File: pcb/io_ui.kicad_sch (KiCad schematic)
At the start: 66 parts, among them J10 UART, J4 Digital IO, J5 ADC Inputs, J8 I2C Bus, Q4 2N7002, Q5 2N7002, U8 24AA64T

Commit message: BOM: fill MPN/Manufacturer/LCSC for 47 Rev B parts (Basic preferred; C3 10u/25V, C7 1u/50V, C11 100n/50V). Hand-solder parts J11, Q3, Q8, DS1, L2 marked Assembly=hand solder and excluded from pos files. Nets unchanged, ERC 0 errors
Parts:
- C22: LCSC (none) -> C49678; MPN (none) -> CC0805KRX7R9BB104; Manufacturer (none) -> YAGEO
- DS1: Assembly (none) -> Hand solder - exclude from JLC assembly; MPN generic 1.3in SH1106 SPI 7-pin -> generic 1.3in SH1106 SPI 7-pin OLED module
- J10, J8: LCSC (none) -> C124378; MPN (none) -> B-2100S04P-A110; Manufacturer (none) -> Ckmtw(Shenzhen Cankemeng)
- J4: LCSC (none) -> C492409; MPN (none) -> PZ254V-11-10P; Manufacturer (none) -> XFCN
- J5: LCSC (none) -> C2840012; MPN (none) -> PZ254V-11-12P; Manufacturer (none) -> XFCN
- Q4, Q5: LCSC (none) -> C8545; MPN (none) -> 2N7002; Manufacturer (none) -> Jiangsu Changjing Electronics Technology
- R11, R12, R14, R15: LCSC (none) -> C26010; MPN (none) -> 0805W8F3301T5E; Manufacturer (none) -> UNI-ROYAL(Uniroyal Elec)
- U8: LCSC (none) -> C2061092; MPN (none) -> 24AA64T-I/OT; Manufacturer (none) -> Microchip Technology

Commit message: S1-S7: Kinghelm KH-6X6X13H-STM 13 mm (C2837539); K5/K6 clear of case-bulkhead strip; gate check 7
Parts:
- S1, S2, S3, S4, S5, S6, S7: LCSC C2837537 -> C2837539; MPN KH-6X6X11H-STM -> KH-6X6X13H-STM
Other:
- note added: "Function keys S1 / S2 / S6 in one row directly under DS1 (as on Si5351AVFO). D-pad cross: S5 Up, S4 Down, S3 Left, S7 Right. Each line: 10k pull-up, 10k series, 100n at the MCU pin (Si5351AVFO network). All switches Kinghelm KH-6X6X13H-STM, pressed = low."
- note removed: "Function keys S1 / S2 / S6 in one row directly under DS1 (as on Si5351AVFO). D-pad cross: S5 Up, S4 Down, S3 Left, S7 Right. Each line: 10k pull-up, 10k series, 100n at the MCU pin (Si5351AVFO network). All switches Kinghelm KH-6X6X11H-STM, pressed = low."
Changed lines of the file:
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@@
 			)
 		)
-		(property "Description" "Tactile switch 6x6 mm SMD, 11 mm actuator (front-panel height, no cap)"
+		(property "Description" "Tactile switch 6x6 mm SMD, 13 mm actuator (front-panel height, no cap)"
 			(at 109.22 26.67 0)
 			(hide yes)
@@
 			)
 		)
-		(property "LCSC" "C2837537"
+		(property "LCSC" "C2837539"
 			(at 109.22 26.67 0)
 			(hide yes)
@@
 			)
 		)
-		(property "MPN" "KH-6X6X11H-STM"
+		(property "MPN" "KH-6X6X13H-STM"
 			(at 109.22 26.67 0)
 			(hide yes)
@@
 			)
 		)
-		(property "Description" "Tactile switch 6x6 mm SMD, 11 mm actuator (front-panel height, no cap)"
+		(property "Description" "Tactile switch 6x6 mm SMD, 13 mm actuator (front-panel height, no cap)"
 			(at 109.22 48.26 0)
 			(hide yes)
@@
 			)
 		)
-		(property "LCSC" "C2837537"
+		(property "LCSC" "C2837539"
 			(at 109.22 48.26 0)
 			(hide yes)
@@
 			)
 		)
-		(property "MPN" "KH-6X6X11H-STM"
+		(property "MPN" "KH-6X6X13H-STM"
 			(at 109.22 48.26 0)
 			(hide yes)
@@
 			)
 		)
-		(property "Description" "Tactile switch 6x6 mm SMD, 11 mm actuator (front-panel height, no cap)"
+		(property "Description" "Tactile switch 6x6 mm SMD, 13 mm actuator (front-panel height, no cap)"
 			(at 109.22 69.85 0)
 			(hide yes)
@@
 			)
 		)
-		(property "LCSC" "C2837537"
+		(property "LCSC" "C2837539"
 			(at 109.22 69.85 0)
 			(hide yes)
@@
 			)
 		)
-		(property "MPN" "KH-6X6X11H-STM"
+		(property "MPN" "KH-6X6X13H-STM"
 			(at 109.22 69.85 0)
 			(hide yes)
@@
 			)
 		)
-		(property "Description" "Tactile switch 6x6 mm SMD, 11 mm actuator (front-panel height, no cap)"
+		(property "Description" "Tactile switch 6x6 mm SMD, 13 mm actuator (front-panel height, no cap)"
 			(at 198.12 26.67 0)
 			(hide yes)
@@
 			)
 		)
-		(property "LCSC" "C2837537"
+		(property "LCSC" "C2837539"
 			(at 198.12 26.67 0)
 			(hide yes)
@@
 			)
 		)
-		(property "MPN" "KH-6X6X11H-STM"
+		(property "MPN" "KH-6X6X13H-STM"
 			(at 198.12 26.67 0)
 			(hide yes)
@@
 			)
 		)
-		(property "Description" "Tactile switch 6x6 mm SMD, 11 mm actuator (front-panel height, no cap)"
+		(property "Description" "Tactile switch 6x6 mm SMD, 13 mm actuator (front-panel height, no cap)"
 			(at 153.67 48.26 0)
 			(hide yes)
@@
 			)
 		)
-		(property "LCSC" "C2837537"
+		(property "LCSC" "C2837539"
 			(at 153.67 48.26 0)
 			(hide yes)
@@
 			)
 		)
-		(property "MPN" "KH-6X6X11H-STM"
+		(property "MPN" "KH-6X6X13H-STM"
 			(at 153.67 48.26 0)
 			(hide yes)
@@
 			)
 		)
-		(property "Description" "Tactile switch 6x6 mm SMD, 11 mm actuator (front-panel height, no cap)"
+		(property "Description" "Tactile switch 6x6 mm SMD, 13 mm actuator (front-panel height, no cap)"
 			(at 242.57 48.26 0)
 			(hide yes)
@@
 			)
 		)
-		(property "LCSC" "C2837537"
+		(property "LCSC" "C2837539"
 			(at 242.57 48.26 0)
 			(hide yes)
@@
 			)
 		)
-		(property "MPN" "KH-6X6X11H-STM"
+		(property "MPN" "KH-6X6X13H-STM"
 			(at 242.57 48.26 0)
 			(hide yes)
@@
 			)
 		)
-		(property "Description" "Tactile switch 6x6 mm SMD, 11 mm actuator (front-panel height, no cap)"
+		(property "Description" "Tactile switch 6x6 mm SMD, 13 mm actuator (front-panel height, no cap)"
 			(at 198.12 69.85 0)
 			(hide yes)
@@
 			)
 		)
-		(property "LCSC" "C2837537"
+		(property "LCSC" "C2837539"
 			(at 198.12 69.85 0)
 			(hide yes)
@@
 			)
 		)
-		(property "MPN" "KH-6X6X11H-STM"
+		(property "MPN" "KH-6X6X13H-STM"
 			(at 198.12 69.85 0)
 			(hide yes)
@@
 		)
 	)
-	(text "Function keys S1 / S2 / S6 in one row directly under DS1\n(as on Si5351AVFO). D-pad cross: S5 Up, S4 Down,\nS3 Left, S7 Right. Each line: 10k pull-up, 10k series,\n100n at the MCU pin (Si5351AVFO network).\nAll switches Kinghelm KH-6X6X11H-STM, pressed = low."
+	(text "Function keys S1 / S2 / S6 in one row directly under DS1\n(as on Si5351AVFO). D-pad cross: S5 Up, S4 Down,\nS3 Left, S7 Right. Each line: 10k pull-up, 10k series,\n100n at the MCU pin (Si5351AVFO network).\nAll switches Kinghelm KH-6X6X13H-STM, pressed = low."
 		(exclude_from_sim no)
 		(at 147.32 20.32 0)

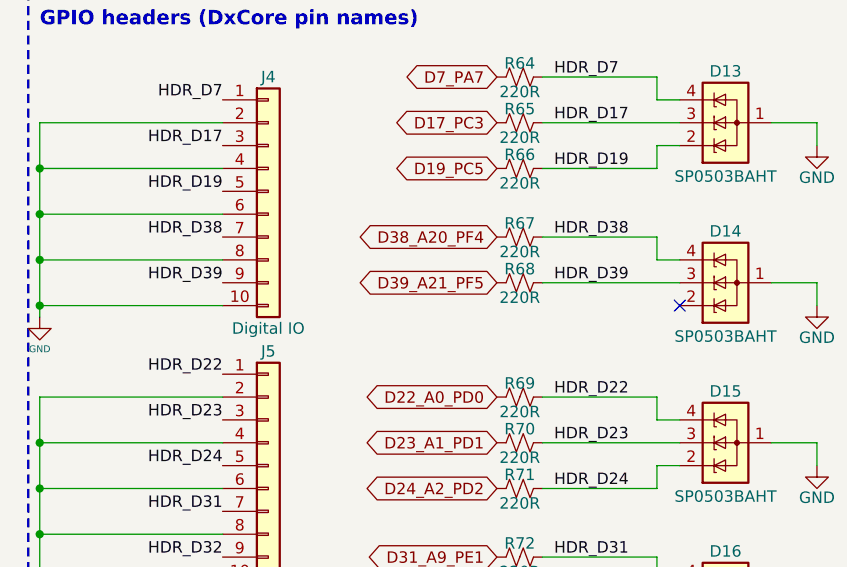
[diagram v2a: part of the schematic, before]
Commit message: GPS_TXD moved to U9 PF5 (pin 39, USART2 RXD ALT1): sch - PB1 NC, R68/HDR_D39 removed, J4.9/D14.3 NC; PCB - GPS_TXD 84 mm west part + new 75 mm east run, torn-up header/LED nets rerouted, HDR_D23 hand-routed, 3 clearance fixes, DRC 0/0; pro netclasses + .NetName DRU + SDA 0.15 mm rule
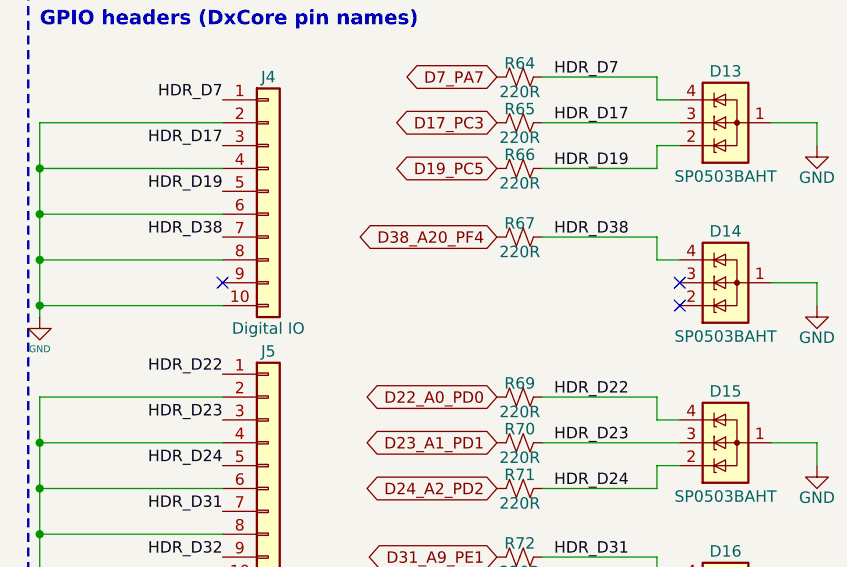
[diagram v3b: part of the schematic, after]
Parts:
- removed R68: 220R, Resistor_SMD:R_0805_2012Metric, symbol Device:R_Small_US
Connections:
- net HDR_D39: no longer names the net of J4.9 (Pin_9)
- net HDR_D39: no longer D14.3 (K)
- no-connect marks 3 -> 5
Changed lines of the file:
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@@
 		)
+	)
+	(no_connect
+		(at 35.56 132.08)
+	)
+	(no_connect
+		(at 86.36 132.08)
 	)
 	(embedded_fonts no)	(label "HDR_D7"
@@
 	(label "HDR_D38"
 		(at 35.56 127 180)
-		(effects
-			(font
-				(size 1.27 1.27)
-			)
-			(justify right bottom)
-		)
-	)
-	(label "HDR_D39"
-		(at 35.56 132.08 180)
 		(effects
 			(font
@@
 		)
 		(stroke
-			(width 0)
-			(type default)
-		)
-	)
-	(global_label "D39_A21_PF5"
-		(shape bidirectional)
-		(at 66.04 132.08 180)
-		(effects
-			(font
-				(size 1.27 1.27)
-			)
-			(justify right)
-		)
-		(property "Intersheetrefs" "${INTERSHEET_REFS}"
-			(at 66.04 132.08 0)
-			(hide yes)
-			(effects
-				(font
-					(size 1.27 1.27)
-				)
-			)
-		)
-	)
-	(symbol
-		(lib_id "Device:R_Small_US")
-		(at 68.58 132.08 90)
-		(unit 1)
-		(exclude_from_sim no)
-		(in_bom yes)
-		(on_board yes)
-		(dnp no)
-		(property "Reference" "R68"
-			(at 68.58 130.556 90)
-			(effects
-				(font
-					(size 1.27 1.27)
-				)
-			)
-		)
-		(property "Value" "220R"
-			(at 68.58 133.731 90)
-			(effects
-				(font
-					(size 1.27 1.27)
-				)
-			)
-		)
-		(property "Footprint" "Resistor_SMD:R_0805_2012Metric"
-			(at 68.58 132.08 0)
-			(effects
-				(font
-					(size 1.27 1.27)
-				)
-				(hide yes)
-			)
-		)
-		(property "Datasheet" ""
-			(at 68.58 132.08 0)
-			(effects
-				(font
-					(size 1.27 1.27)
-				)
-				(hide yes)
-			)
-		)
-		(property "LCSC" "C17557"
-			(at 68.58 132.08 0)
-			(effects
-				(font
-					(size 1.27 1.27)
-				)
-				(hide yes)
-			)
-		)
-		(property "MPN" "0805W8F2200T5E"
-			(at 68.58 132.08 0)
-			(effects
-				(font
-					(size 1.27 1.27)
-				)
-				(hide yes)
-			)
-		)
-		(property "Manufacturer" "UNI-ROYAL"
-			(at 68.58 132.08 0)
-			(effects
-				(font
-					(size 1.27 1.27)
-				)
-				(hide yes)
-			)
-		)
-		(pin "1"
-		)
-		(pin "2"
-		)
-		(instances
-			(project "OpenBeacon2"
-				(path "/046319a3-a6ce-4e59-a888-94e340127381/b6e1d2a4-3c5f-4e7a-8d90-1f2a3b4c5d6e"
-					(reference "R68")
-					(unit 1)
-				)
-			)
-		)
-	)
-	(label "HDR_D39"
-		(at 72.39 132.08 0)
-		(effects
-			(font
-				(size 1.27 1.27)
-			)
-			(justify left bottom)
-		)
-	)
-	(wire
-		(pts
-			(xy 71.12 132.08) (xy 86.36 132.08)
-		)
-		(stroke

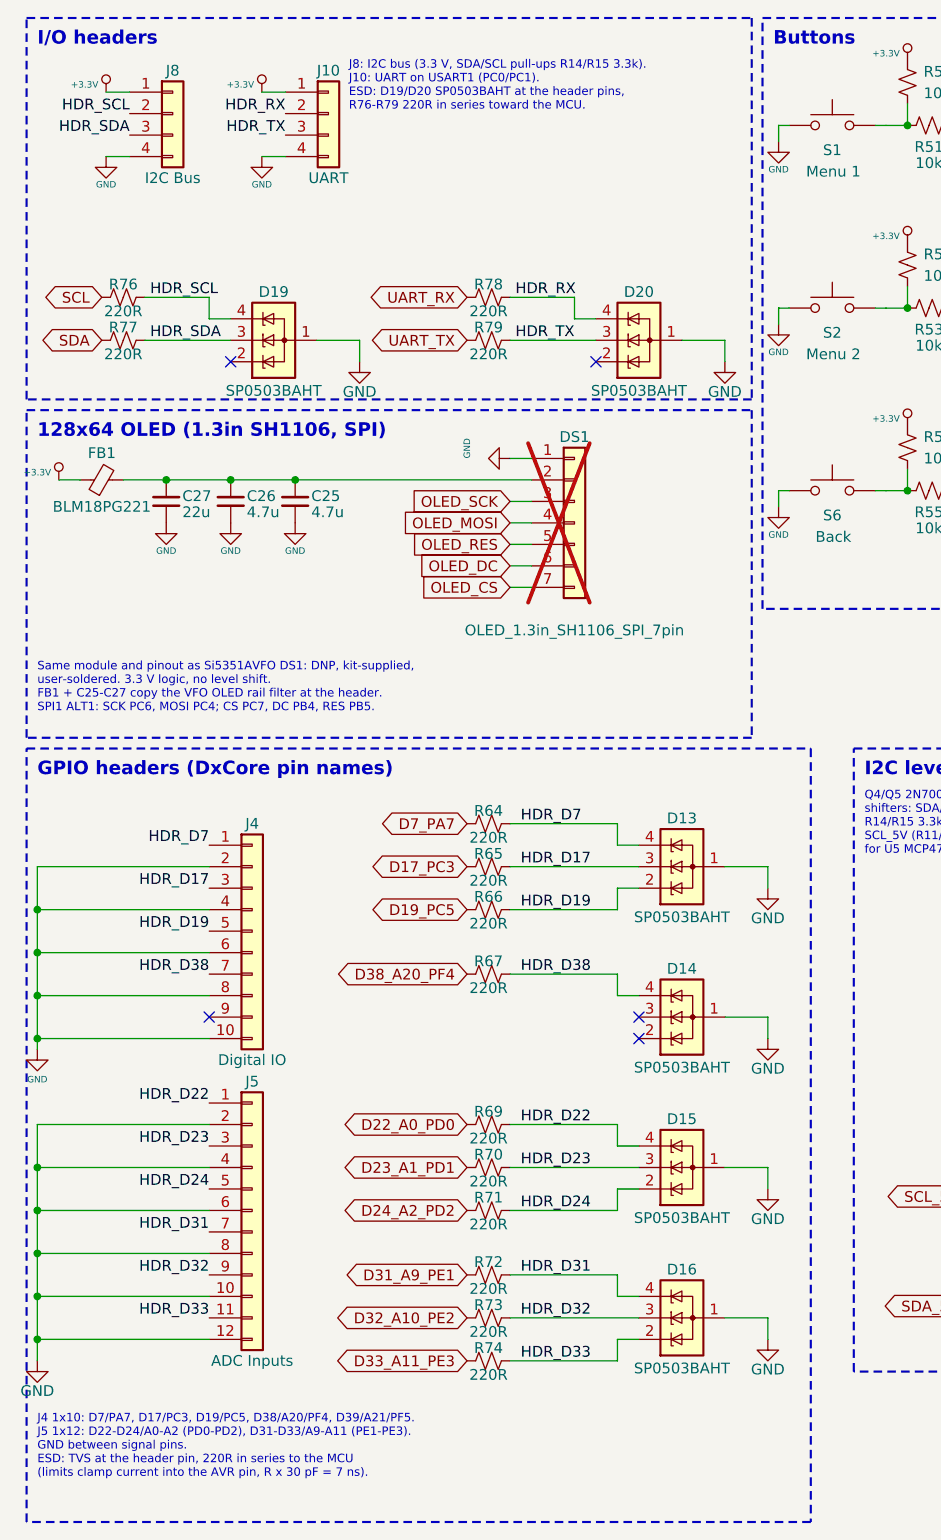
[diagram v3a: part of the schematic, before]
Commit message: Rev C layout: board grown to 130x110 mm, headers J4/J5/J8/J10/J14 removed, power rework layout
- Outline grown 10 mm on top and left edges (130x110 mm); locked edge parts moved with outline
- Removed J4, J5, J8, J10, J14 and support parts (D13-D15, D17, D19, D20, R64-R67, R69-R71, R75-R79); UPDI J13 kept
- Power rework placed and routed (TPS61085 boost, INA193 U14, Q10 soft-start)
- Y1 placed at U9, stray passives moved, silkscreen labels cleaned up
- Routed: DRC 0 errors / 0 unconnected, schematic parity 0, ERC 0; layout gate 11/11
- DRU: ESC_* fine-pitch escape 0.20 mm rule areas, U1 pad-to-pad 0.14 mm
- In2 keep-away waivers (GND-plane shielded): Q2 drain, MCU_TX, MCU_RX near R6, 22.6 mm MCU_RX run near U9
- Libs: 6x6 H13 switch, OLED pin-header module footprint, updated symbols
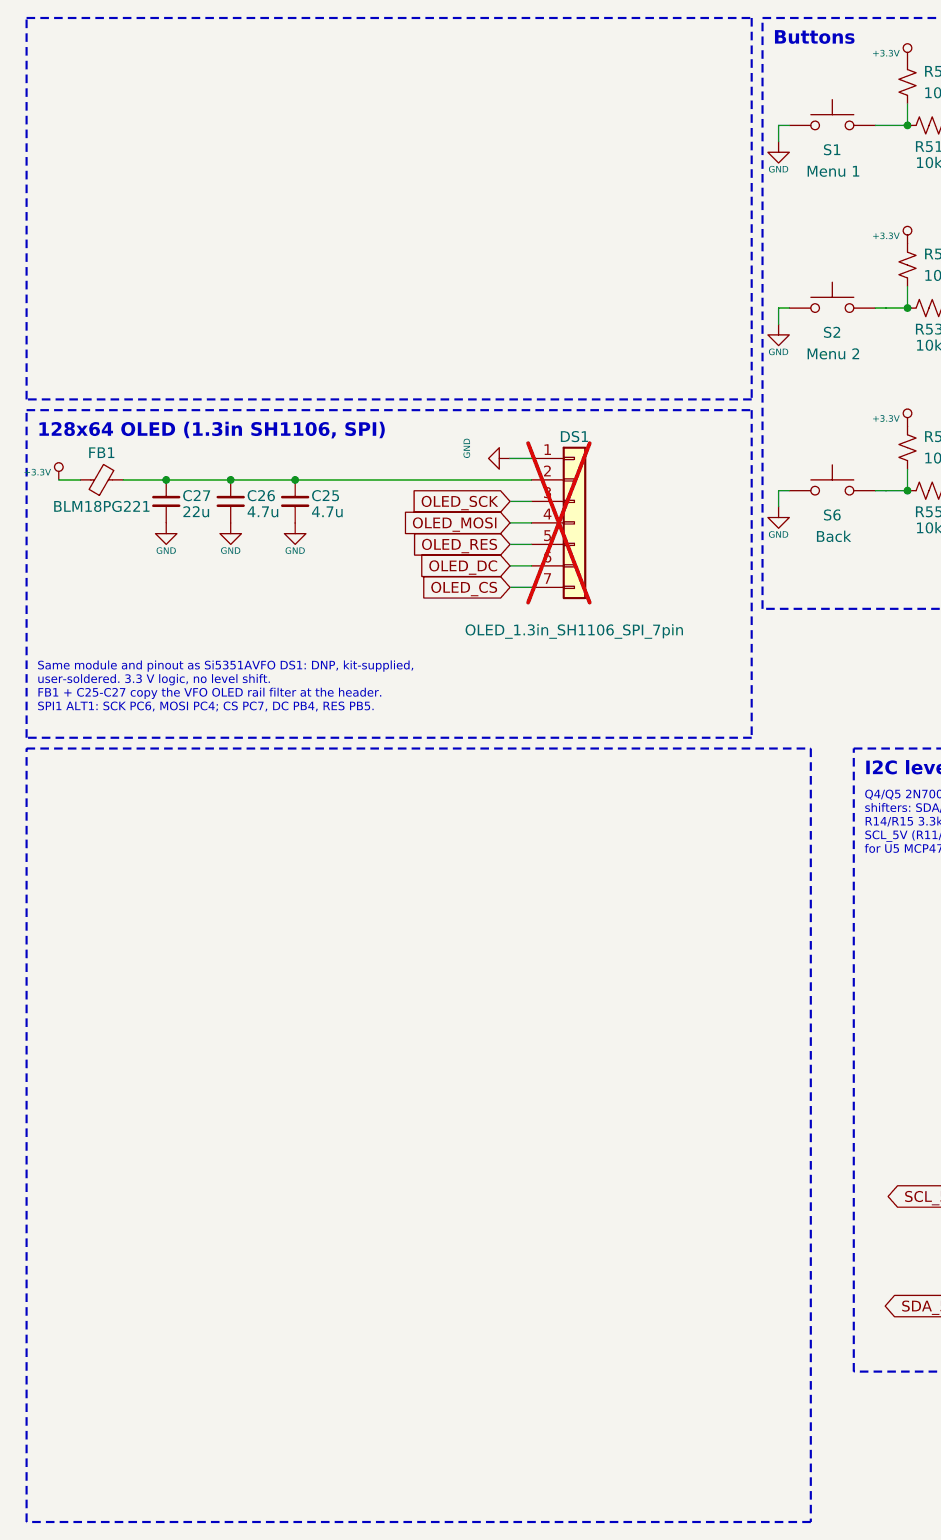
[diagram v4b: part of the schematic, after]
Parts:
- removed D13, D14, D15, D16, D19, D20: SP0503BAHT, Package_TO_SOT_SMD:SOT-143, symbol Power_Protection:SP0503BAHT
- removed J10: UART, Connector_PinHeader_2.54mm:PinHeader_1x04_P2.54mm_Vertical, symbol Connector_Generic:Conn_01x04
- removed J4: Digital IO, Connector_PinHeader_2.54mm:PinHeader_1x10_P2.54mm_Vertical, symbol Connector_Generic:Conn_01x10
- removed J5: ADC Inputs, Connector_PinHeader_2.54mm:PinHeader_1x12_P2.54mm_Vertical, symbol Connector_Generic:Conn_01x12
- removed J8: I2C Bus, Connector_PinHeader_2.54mm:PinHeader_1x04_P2.54mm_Vertical, symbol Connector_Generic:Conn_01x04
- removed R64, R65, R66, R67, R69, R70, R71, R72, R73, R74, R76, R77, R78, R79: 220R, Resistor_SMD:R_0805_2012Metric, symbol Device:R_Small_US
- DS1: footprint Connector_PinHeader_2.54mm:PinHeader_1x07_P2.54mm_Vertical -> OB2:OLED_1.3in_SH1106_PinHeader_1x07_P2.54mm
- S1, S2, S3, S4, S5, S6, S7: footprint OB2:SW_Push_6x6mm_SMD_KH-6X6X11H-STM -> OB2:SW_Push_6x6mm_SMD_KH-6X6X13H-STM
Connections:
- no-connect marks 5 -> 0
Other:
- note removed: "GPIO headers (DxCore pin names)"
- note removed: "I/O headers"
- note removed: "J4 1x10: D7/PA7, D17/PC3, D19/PC5, D38/A20/PF4, D39/A21/PF5. J5 1x12: D22-D24/A0-A2 (PD0-PD2), D31-D33/A9-A11 (PE1-PE3). GND between signal pins. ESD: TVS at the header pin, 220R in series to the MCU (limits clamp current into the AVR pin, R x 30 pF = 7 ns)."
- note removed: "J8: I2C bus (3.3 V, SDA/SCL pull-ups R14/R15 3.3k). J10: UART on USART1 (PC0/PC1). ESD: D19/D20 SP0503BAHT at the header pins, R76-R79 220R in series toward the MCU."

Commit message: Renumber all references monotonically 1..N per prefix; sync PCB silk labels and auto-named nets; ERC 0, DRC 0/0
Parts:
- renumbered C17 to C108, C21 to C109, C19 to C110, C18 to C111, C24 to C112, C27 to C113, C26 to C114, C25 to C115, C23 to C116, C20 to C117, C22 to C118, Q4 to Q10, Q5 to Q9, R50 to R43, R56 to R44, R51 to R45, R57 to R46, R52 to R47, R58 to R48, R60 to R49, R53 to R50, R59 to R51, R61 to R52, R54 to R53, R62 to R54, R63 to R56, R14 to R57, R15 to R58, R11 to R59, R12 to R60, S5 to S2, S2 to S3, S3 to S4, S7 to S5, S4 to S7, U8 to U12
